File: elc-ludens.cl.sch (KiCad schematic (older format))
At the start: 48 parts, among them P1 CONN_2, P2 CONN_2, P3 CONN_2, P4 CONN_8, Q1 BC337, Q2 BC337, Q3 BC337, Q4 BC337, Q5 BC337, Q6 BC337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

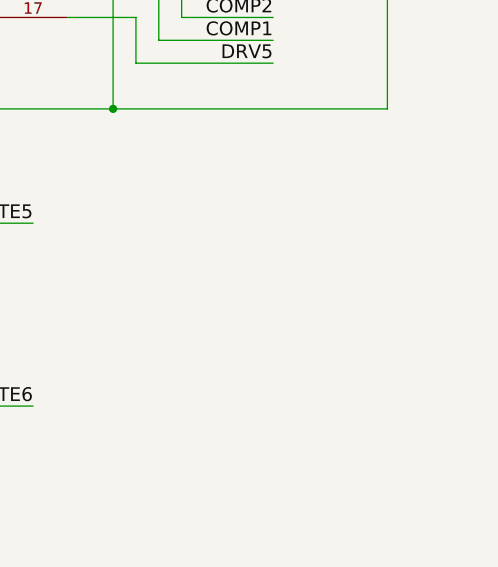
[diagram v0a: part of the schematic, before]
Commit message: Tidy PCB and add Fixing Holes
Must use nylon/plastic hardware to use the fixing holes
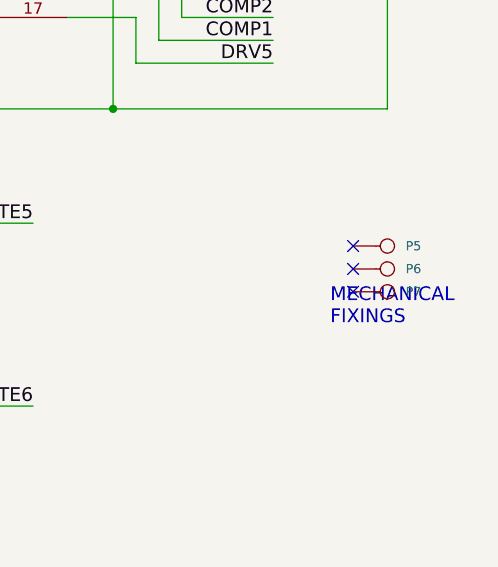
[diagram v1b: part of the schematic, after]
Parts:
- added P5, P6, P7: CONN_1, symbol CONN_1
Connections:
- no-connect marks 2 -> 5
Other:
- note added: "MECHANICAL\nFIXINGS"
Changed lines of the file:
@@
-EESchema Schematic File Version 2  date 02/01/2014 17:04:41
+EESchema Schematic File Version 2  date 03/01/2014 12:24:21
 LIBS:power
 LIBS:device
@@
 LIBS:contrib
 LIBS:valves
+LIBS:elc-ludens.cl-cache
 EELAYER 27 0
 EELAYER END
@@
 Sheet 1 1
 Title "ELC"
-Date "2 jan 2014"
+Date "3 jan 2014"
 Rev "1"
 Comp ""
@@
 	4100 2400 4100 2450
 Connection ~ 4100 2450
+$Comp
+L CONN_1 P5
+U 1 1 52C6AE40
+P 10500 3800
+F 0 "P5" H 10580 3800 40  0000 L CNN
+F 1 "CONN_1" H 10500 3855 30  0001 C CNN
+F 2 "" H 10500 3800 60  0000 C CNN
+F 3 "" H 10500 3800 60  0000 C CNN
+	1    10500 3800
+	1    0    0    -1
+$EndComp
+$Comp
+L CONN_1 P6
+U 1 1 52C6AE4F
+P 10500 3900
+F 0 "P6" H 10580 3900 40  0000 L CNN
+F 1 "CONN_1" H 10500 3955 30  0001 C CNN
+F 2 "" H 10500 3900 60  0000 C CNN
+F 3 "" H 10500 3900 60  0000 C CNN
+	1    10500 3900
+	1    0    0    -1
+$EndComp
+$Comp
+L CONN_1 P7
+U 1 1 52C6AE5E
+P 10500 4000
+F 0 "P7" H 10580 4000 40  0000 L CNN
+F 1 "CONN_1" H 10500 4055 30  0001 C CNN
+F 2 "" H 10500 4000 60  0000 C CNN
+F 3 "" H 10500 4000 60  0000 C CNN
+	1    10500 4000
+	1    0    0    -1
+$EndComp
+Text Notes 10250 4150 0    60   ~ 0
+MECHANICAL\nFIXINGS
+NoConn ~ 10350 4000
+NoConn ~ 10350 3900
+NoConn ~ 10350 3800
 $EndSCHEMATC

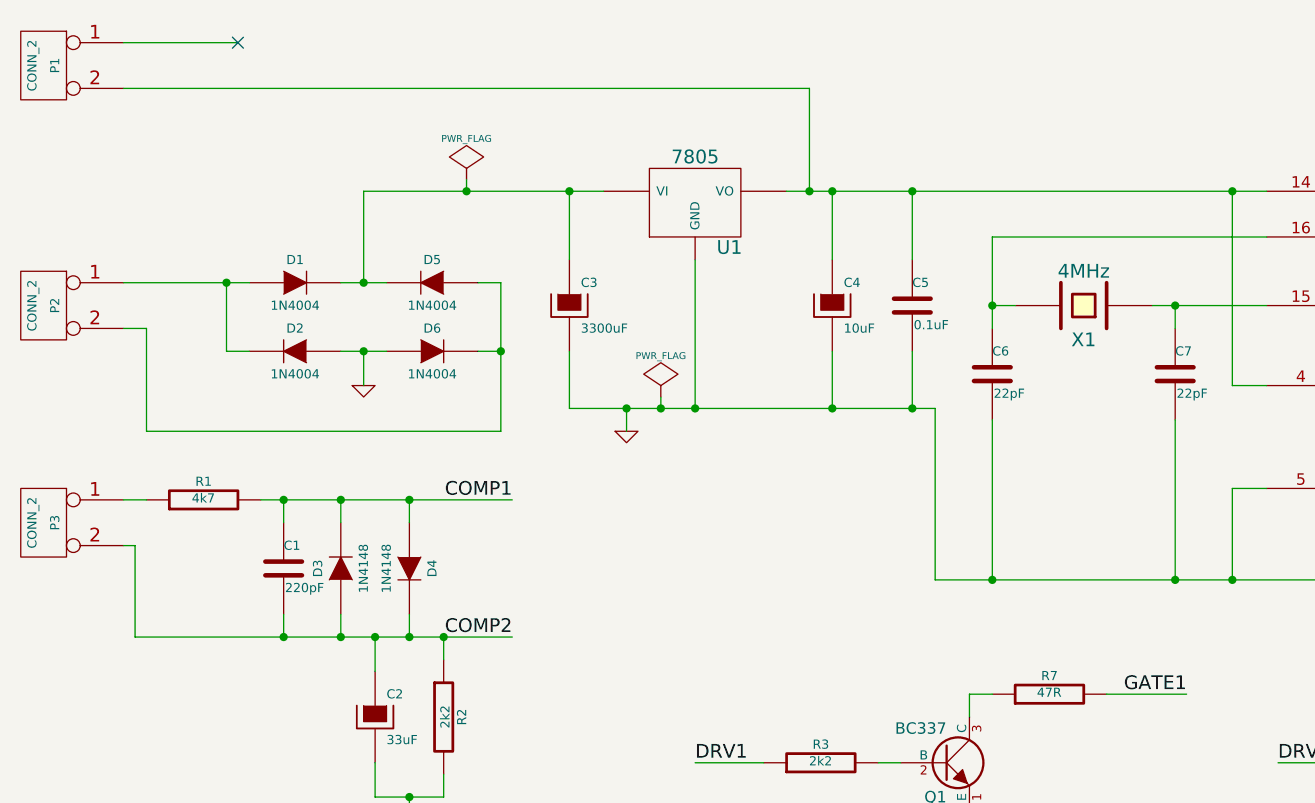
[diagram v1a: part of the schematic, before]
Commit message: Add missing resistor
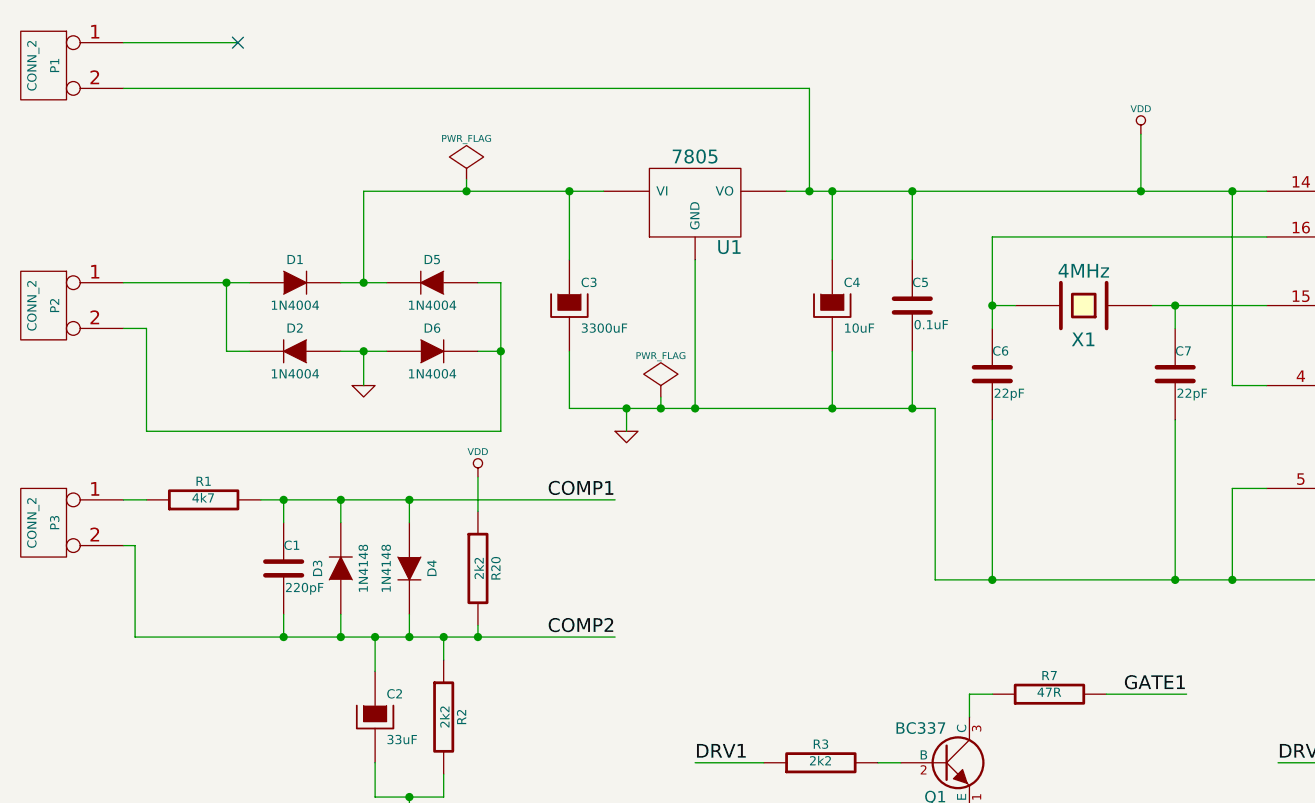
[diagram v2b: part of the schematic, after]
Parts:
- added R20: 2k2, ~, symbol R
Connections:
- net COMP2: now also R20.2
- net VDD: now reaches C4.1, C5.1, P1.2 (PM), U1.VO, U2.14 (VDD), U2.4 (MCLR)
- net VDD: now also R20.1
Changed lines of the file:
@@
-EESchema Schematic File Version 2  date 03/01/2014 12:24:21
+EESchema Schematic File Version 2  date 06/01/2014 17:26:26
 LIBS:power
 LIBS:device
@@
 Sheet 1 1
 Title "ELC"
-Date "3 jan 2014"
+Date "6 jan 2014"
 Rev "1"
 Comp ""
@@
 $EndComp
 Wire Wire Line
-	2350 2850 3450 2850
+	2350 2850 3900 2850
 Wire Wire Line
 	2450 2850 2450 2950
@@
 	1800 3050 1800 3450
 Wire Wire Line
-	1800 3450 3450 3450
+	1800 3450 3900 3450
 Wire Wire Line
 	2450 3450 2450 3350
@@
 Connection ~ 3000 2850
 Connection ~ 3150 3450
-Text Label 3450 2850 2    60   ~ 0
+Text Label 3900 2850 2    60   ~ 0
 COMP1
-Text Label 3450 3450 2    60   ~ 0
+Text Label 3900 3450 2    60   ~ 0
 COMP2
 Wire Wire Line
@@
 NoConn ~ 10350 3900
 NoConn ~ 10350 3800
+$Comp
+L R R20
+U 1 1 52CAE96A
+P 3300 3150
+F 0 "R20" V 3380 3150 40  0000 C CNN
+F 1 "2k2" V 3307 3151 40  0000 C CNN
+F 2 "~" V 3230 3150 30  0000 C CNN
+F 3 "~" H 3300 3150 30  0000 C CNN
+	1    3300 3150
+	1    0    0    -1
+$EndComp
+$Comp
+L VDD #PWR014
+U 1 1 52CAE979
+P 6200 1250
+F 0 "#PWR014" H 6200 1350 30  0001 C CNN
+F 1 "VDD" H 6200 1360 30  0000 C CNN
+F 2 "" H 6200 1250 60  0000 C CNN
+F 3 "" H 6200 1250 60  0000 C CNN
+	1    6200 1250
+	1    0    0    -1
+$EndComp
+Wire Wire Line
+	6200 1250 6200 1500
+Connection ~ 6200 1500
+$Comp
+L VDD #PWR015
+U 1 1 52CAEAD8
+P 3300 2750
+F 0 "#PWR015" H 3300 2850 30  0001 C CNN
+F 1 "VDD" H 3300 2860 30  0000 C CNN
+F 2 "" H 3300 2750 60  0000 C CNN
+F 3 "" H 3300 2750 60  0000 C CNN
+	1    3300 2750
+	1    0    0    -1
+$EndComp
+Wire Wire Line
+	3300 2900 3300 2750
+Wire Wire Line
+	3300 3400 3300 3450
+Connection ~ 3300 3450
 $EndSCHEMATC

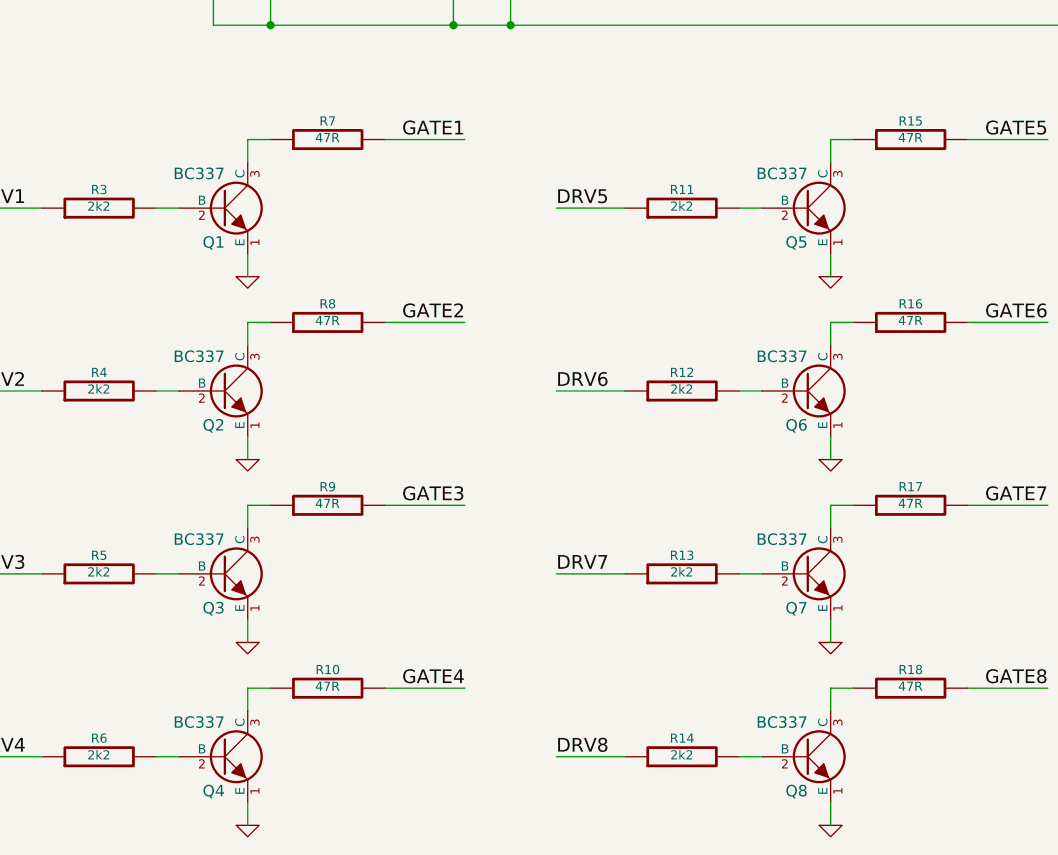
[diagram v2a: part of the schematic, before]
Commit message: Layout fix BC337 pinout + Add resistor
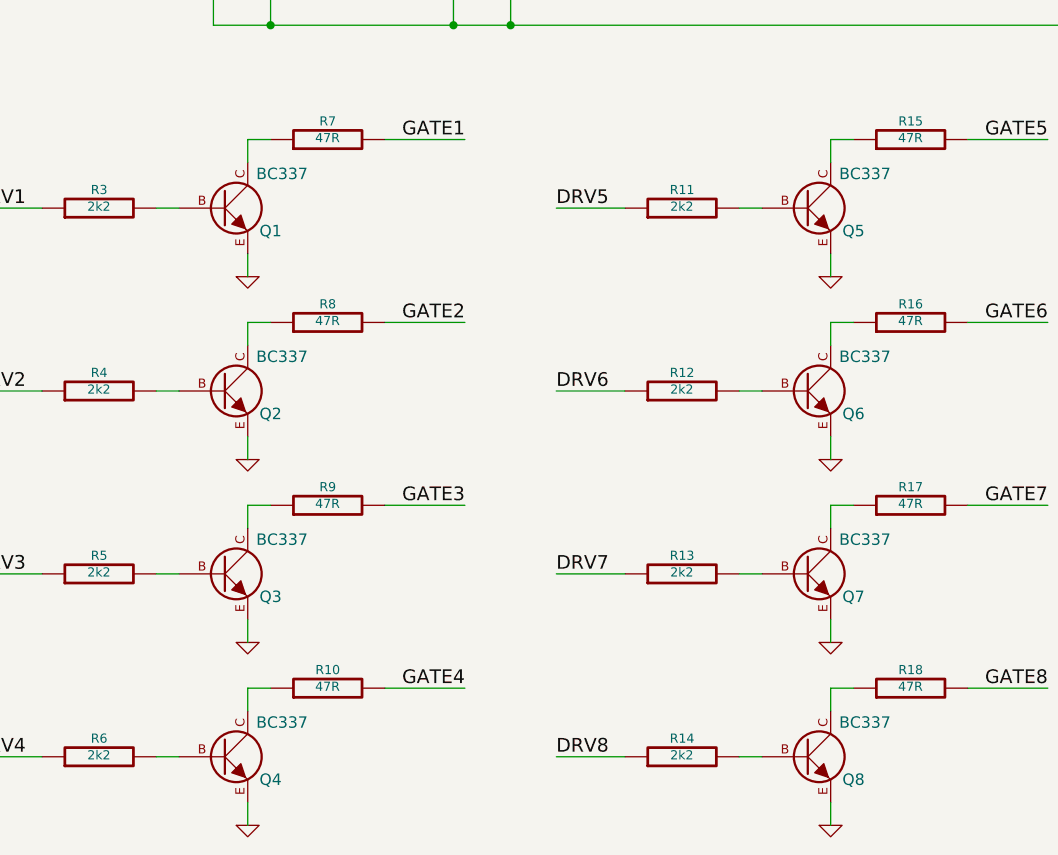
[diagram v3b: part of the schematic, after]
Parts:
- removed Q1, Q2, Q3, Q4, Q5, Q6, Q7, Q8: BC337, ~, symbol NPN
- added Q1, Q2, Q3, Q4, Q5, Q6, Q7, Q8: BC337, TO92-EBC, symbol BC237
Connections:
- net GND: now also Q1.E, Q2.E, Q3.E, Q4.E, Q5.E, Q6.E, Q7.E, Q8.E
- net at R3.2: now also Q1.B
- net at R7.1: now also Q1.C
- net at R4.2: now also Q2.B
- net at R8.1: now also Q2.C
- net at R5.2: now also Q3.B
- net at R9.1: now also Q3.C
- net at R6.2: now also Q4.B
- net at R10.1: now also Q4.C
- net at R11.2: now also Q5.B
- net at R15.1: now also Q5.C
- net at R12.2: now also Q6.B
- net at R16.1: now also Q6.C
- net at R13.2: now also Q7.B
- net at R17.1: now also Q7.C
- net at R14.2: now also Q8.B
- net at R18.1: now also Q8.C
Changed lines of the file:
@@
-EESchema Schematic File Version 2  date 06/01/2014 17:26:26
+EESchema Schematic File Version 2  date 17/01/2014 12:33:18
 LIBS:power
 LIBS:device
@@
 Sheet 1 1
 Title "ELC"
-Date "6 jan 2014"
+Date "17 jan 2014"
 Rev "1"
 Comp ""
@@
 	9600 2800 10000 2800
 $Comp
-L NPN Q1
-U 1 1 52C5648F
-P 5350 4000
-F 0 "Q1" H 5350 3850 50  0000 R CNN
-F 1 "BC337" H 5350 4150 50  0000 R CNN
-F 2 "~" H 5350 4000 60  0000 C CNN
-F 3 "~" H 5350 4000 60  0000 C CNN
-F 4 "1228215" H 5350 4000 60  0001 C CNN "Farnell"
-	1    5350 4000
-	1    0    0    -1
-$EndComp
-$Comp
 L R R3
 U 1 1 52C5649E
@@
 Wire Wire Line
 	5450 3700 5450 3800
-Wire Wire Line
-	5150 4000 5050 4000
 $Comp
 L GND #PWR04
@@
 Text Label 4250 4000 0    60   ~ 0
 DRV1
-$Comp
-L NPN Q2
-U 1 1 52C56701
-P 5350 4800
-F 0 "Q2" H 5350 4650 50  0000 R CNN
-F 1 "BC337" H 5350 4950 50  0000 R CNN
-F 2 "~" H 5350 4800 60  0000 C CNN
-F 3 "~" H 5350 4800 60  0000 C CNN
-F 4 "1228215" H 5350 4800 60  0001 C CNN "Farnell"
-	1    5350 4800
-	1    0    0    -1
-$EndComp
 $Comp
 L R R4
@@
 DRV2
 $Comp
-L NPN Q3
-U 1 1 52C56721
-P 5350 5600
-F 0 "Q3" H 5350 5450 50  0000 R CNN
-F 1 "BC337" H 5350 5750 50  0000 R CNN
-F 2 "~" H 5350 5600 60  0000 C CNN
-F 3 "~" H 5350 5600 60  0000 C CNN
-F 4 "1228215" H 5350 5600 60  0001 C CNN "Farnell"
-	1    5350 5600
-	1    0    0    -1
-$EndComp
-$Comp
 L R R5
 U 1 1 52C56727
@@
 DRV3
 $Comp
-L NPN Q4
-U 1 1 52C56741
-P 5350 6400
-F 0 "Q4" H 5350 6250 50  0000 R CNN
-F 1 "BC337" H 5350 6550 50  0000 R CNN
-F 2 "~" H 5350 6400 60  0000 C CNN
-F 3 "~" H 5350 6400 60  0000 C CNN
-F 4 "1228215" H 5350 6400 60  0001 C CNN "Farnell"
-	1    5350 6400
-	1    0    0    -1
-$EndComp
-$Comp
 L R R6
 U 1 1 52C56747
@@
 DRV4
 $Comp
-L NPN Q5
-U 1 1 52C56761
-P 7900 4000
-F 0 "Q5" H 7900 3850 50  0000 R CNN
-F 1 "BC337" H 7900 4150 50  0000 R CNN
-F 2 "~" H 7900 4000 60  0000 C CNN
-F 3 "~" H 7900 4000 60  0000 C CNN
-F 4 "1228215" H 7900 4000 60  0001 C CNN "Farnell"
-	1    7900 4000
-	1    0    0    -1
-$EndComp
-$Comp
 L R R11
 U 1 1 52C56767
@@
 DRV5
 $Comp
-L NPN Q6
-U 1 1 52C56781
-P 7900 4800
-F 0 "Q6" H 7900 4650 50  0000 R CNN
-F 1 "BC337" H 7900 4950 50  0000 R CNN
-F 2 "~" H 7900 4800 60  0000 C CNN
-F 3 "~" H 7900 4800 60  0000 C CNN
-F 4 "1228215" H 7900 4800 60  0001 C CNN "Farnell"
-	1    7900 4800
-	1    0    0    -1
-$EndComp
-$Comp
 L R R12
 U 1 1 52C56787
@@
 DRV6
 $Comp
-L NPN Q7
-U 1 1 52C567A1
-P 7900 5600
-F 0 "Q7" H 7900 5450 50  0000 R CNN
-F 1 "BC337" H 7900 5750 50  0000 R CNN
-F 2 "~" H 7900 5600 60  0000 C CNN
-F 3 "~" H 7900 5600 60  0000 C CNN
-F 4 "1228215" H 7900 5600 60  0001 C CNN "Farnell"
-	1    7900 5600
-	1    0    0    -1
-$EndComp
-$Comp
 L R R13
 U 1 1 52C567A7
@@
 Text Label 6800 5600 0    60   ~ 0
 DRV7
-$Comp
-L NPN Q8
-U 1 1 52C567C1
-P 7900 6400
-F 0 "Q8" H 7900 6250 50  0000 R CNN
-F 1 "BC337" H 7900 6550 50  0000 R CNN
-F 2 "~" H 7900 6400 60  0000 C CNN
-F 3 "~" H 7900 6400 60  0000 C CNN
-F 4 "1228215" H 7900 6400 60  0001 C CNN "Farnell"
-	1    7900 6400
-	1    0    0    -1
-$EndComp
 $Comp
 L R R14
@@
 	3300 3400 3300 3450
 Connection ~ 3300 3450
+$Comp
+L BC237 Q1
+U 1 1 52D92174
+P 5350 4000
+F 0 "Q1" H 5550 3900 50  0000 C CNN
+F 1 "BC337" H 5600 4150 50  0000 C CNN
+F 2 "TO92-EBC" H 5540 4000 30  0001 C CNN
+F 3 "~" H 5350 4000 60  0000 C CNN
+	1    5350 4000
+	1    0    0    -1
+$EndComp
+$Comp
+L BC237 Q2
+U 1 1 52D92183
+P 5350 4800
+F 0 "Q2" H 5550 4700 50  0000 C CNN
+F 1 "BC337" H 5600 4950 50  0000 C CNN
+F 2 "TO92-EBC" H 5540 4800 30  0001 C CNN
+F 3 "~" H 5350 4800 60  0000 C CNN
+	1    5350 4800
+	1    0    0    -1
+$EndComp
+$Comp
+L BC237 Q3
+U 1 1 52D92192
+P 5350 5600
+F 0 "Q3" H 5550 5500 50  0000 C CNN
+F 1 "BC337" H 5600 5750 50  0000 C CNN
+F 2 "TO92-EBC" H 5540 5600 30  0001 C CNN
+F 3 "~" H 5350 5600 60  0000 C CNN
+	1    5350 5600
+	1    0    0    -1
+$EndComp
+$Comp
+L BC237 Q4
+U 1 1 52D921A1
+P 5350 6400
+F 0 "Q4" H 5550 6300 50  0000 C CNN
+F 1 "BC337" H 5600 6550 50  0000 C CNN
+F 2 "TO92-EBC" H 5540 6400 30  0001 C CNN
+F 3 "~" H 5350 6400 60  0000 C CNN
+	1    5350 6400
+	1    0    0    -1
+$EndComp
+$Comp
+L BC237 Q8
+U 1 1 52D921B0
+P 7900 6400
+F 0 "Q8" H 8100 6300 50  0000 C CNN
+F 1 "BC337" H 8150 6550 50  0000 C CNN
+F 2 "TO92-EBC" H 8090 6400 30  0001 C CNN
+F 3 "~" H 7900 6400 60  0000 C CNN
+	1    7900 6400
+	1    0    0    -1
+$EndComp
+$Comp
+L BC237 Q7
+U 1 1 52D921BF
+P 7900 5600
+F 0 "Q7" H 8100 5500 50  0000 C CNN
+F 1 "BC337" H 8150 5750 50  0000 C CNN
+F 2 "TO92-EBC" H 8090 5600 30  0001 C CNN
+F 3 "~" H 7900 5600 60  0000 C CNN
+	1    7900 5600
+	1    0    0    -1
+$EndComp
+$Comp
+L BC237 Q6
+U 1 1 52D921CE
+P 7900 4800
+F 0 "Q6" H 8100 4700 50  0000 C CNN
+F 1 "BC337" H 8150 4950 50  0000 C CNN
+F 2 "TO92-EBC" H 8090 4800 30  0001 C CNN
+F 3 "~" H 7900 4800 60  0000 C CNN
+	1    7900 4800
+	1    0    0    -1
+$EndComp
+$Comp
+L BC237 Q5
+U 1 1 52D921DD
+P 7900 4000
+F 0 "Q5" H 8100 3900 50  0000 C CNN
+F 1 "BC337" H 8150 4150 50  0000 C CNN
+F 2 "TO92-EBC" H 8090 4000 30  0001 C CNN
+F 3 "~" H 7900 4000 60  0000 C CNN
+	1    7900 4000
+	1    0    0    -1
+$EndComp
+Wire Wire Line
+	5150 4000 5050 4000
 $EndSCHEMATC

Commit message: Finalise PCB Design and produce production gerbers
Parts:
- Q1, Q2, Q3, Q4, Q5, Q6, Q8: Farnell (none) -> 1574379
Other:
- moved on the sheet: C1, C2, C3, C4, C5, C6, C7, D1, D2, D3, D4, D5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
